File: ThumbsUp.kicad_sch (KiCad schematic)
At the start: 45 parts, among them J10 Raiser_Male, J13 Raiser_Female, J14 Raiser_Male, J19 Raiser_Female, J1L1 PJ-3200B, J1R1 PJ-3200B, J33 Raiser_Male, J34 Raiser_Female, J35 Raiser_Male, J38 Raiser_Female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

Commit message: K12: Placed the touchpad, todo: tracks
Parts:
- added J1, J2: 52559-1233, KiCad:525591233, symbol ThumbsUp-rescue:52559-1233-52559-1233
- added R1, R2, R4, R5: 4.7k, Resistor_SMD:R_0805_2012Metric, symbol Device:R_Small
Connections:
- net GND: now also J1.11, J2.11
- net SDA: now reaches U1.5 (SDA)
- net SDA: now also J1.10, J2.10, R1.1, R5.1
- net SCL: now reaches U1.6 (SCL)
- net SCL: now also J1.9, J2.9, R2.2, R4.2
- new net +3.3V: R1.2, R2.1, R4.1, R5.2
- new net VCC: J1.12, J2.12
- no-connect marks 0 -> 24
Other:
- note added: "Cirque Trackpad Connectors"
- note added: "Dummy network for the shielding/fill-in areas, separating them from the ground line."
- note added: "Pull-up for Cirque Trackpad Resistors are repeated twice - to place their location on both sides."
- moved on the sheet: JP1, R17

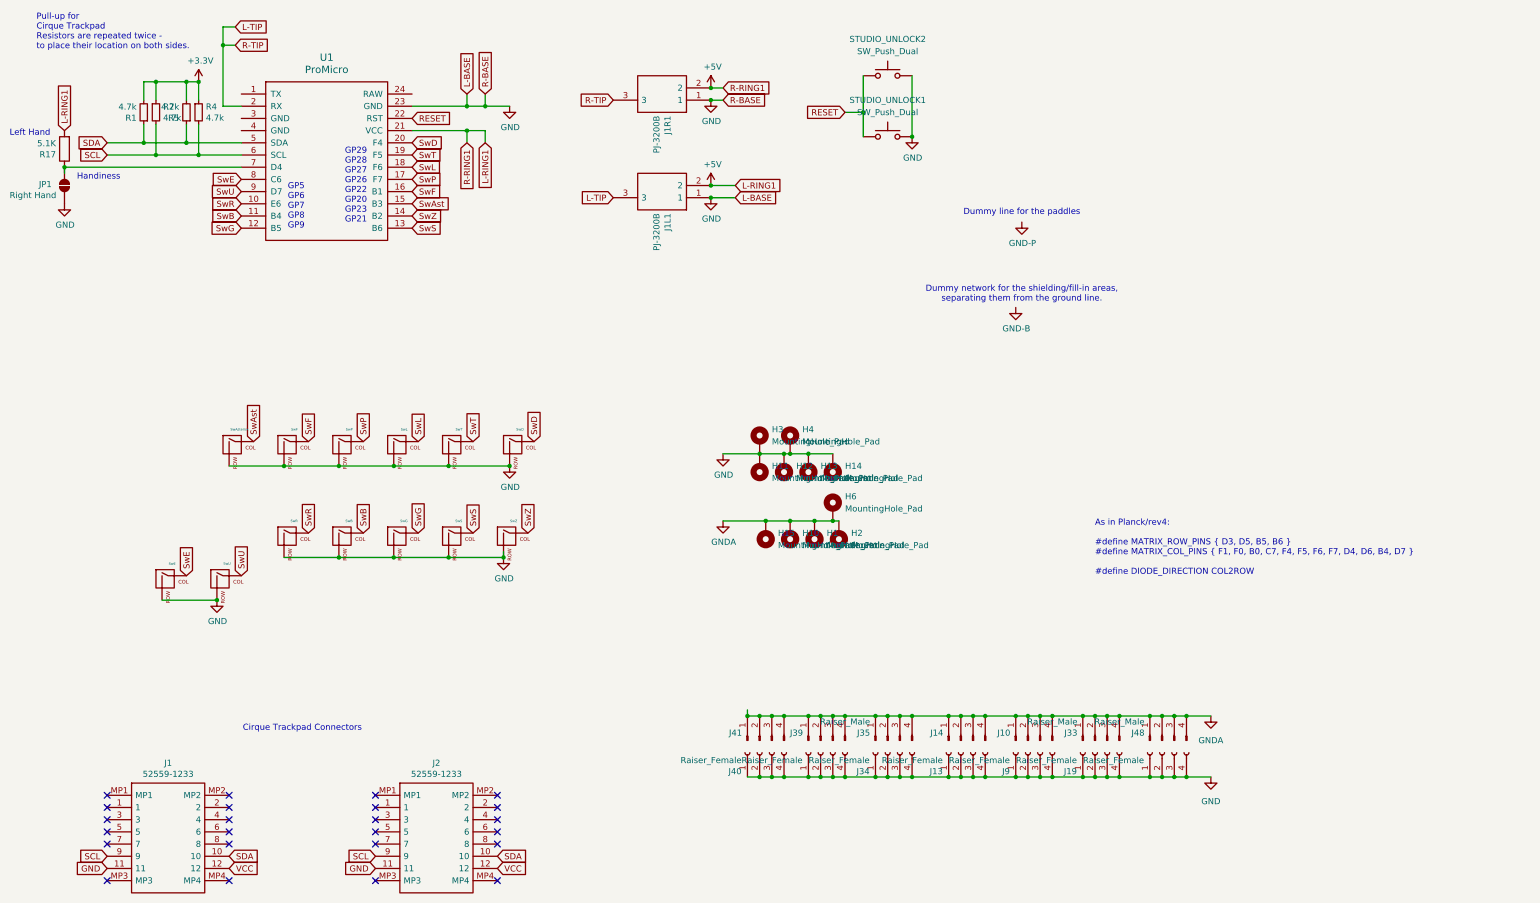
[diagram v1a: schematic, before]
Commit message: K12: Placed the tracks, text, etc. TODO: generate Gerbers.
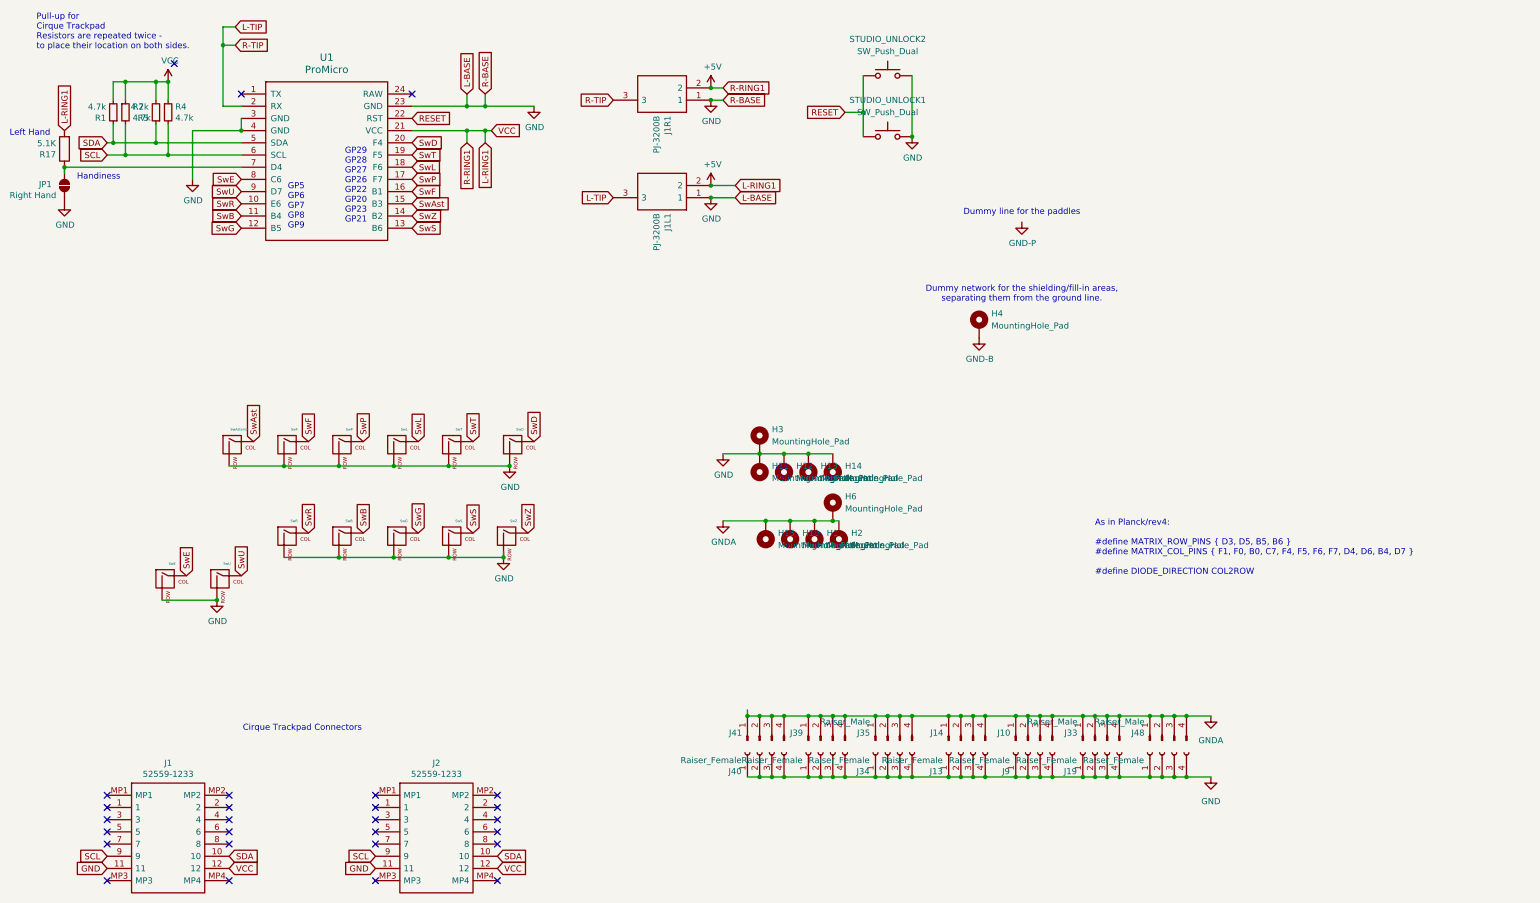
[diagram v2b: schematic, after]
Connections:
- net +3.3V is gone; now on net +5V: R1.2, R2.1, R4.1, R5.2
- net VCC is gone; now on net +5V: J1.12, J2.12
- net GND: now also U1.3 (GND), U1.4 (GND); no longer H4.1
- net GND-B: now also H4.1
- no-connect marks 24 -> 27
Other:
- moved on the sheet: H4, R1, R2, R4, R5

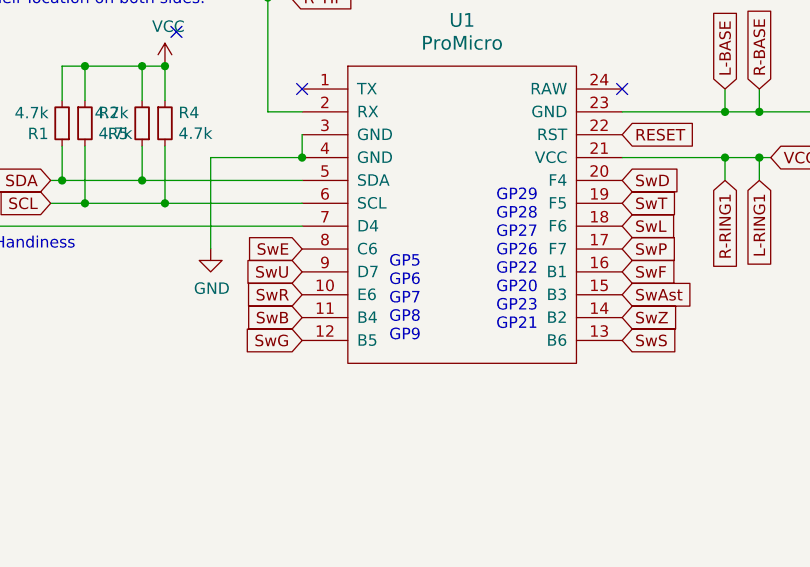
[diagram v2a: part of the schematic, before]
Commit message: K12: Added pictures of rev.3.
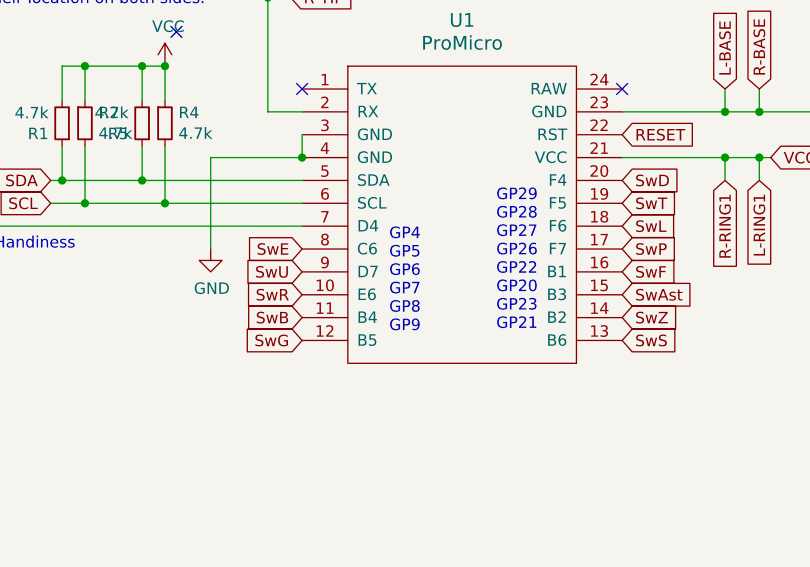
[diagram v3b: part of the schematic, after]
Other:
- note added: "GP4 GP5 GP6 GP7 GP8 GP9"
- note removed: "GP5 GP6 GP7 GP8 GP9"
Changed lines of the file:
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@@
 		)
 	)
-	(text "GP5\nGP6\nGP7\nGP8\nGP9"
+	(text "GP4\nGP5\nGP6\nGP7\nGP8\nGP9"
 		(exclude_from_sim no)
-		(at 320.04 226.568 0)
+		(at 320.04 224.536 0)
 		(effects
 			(font

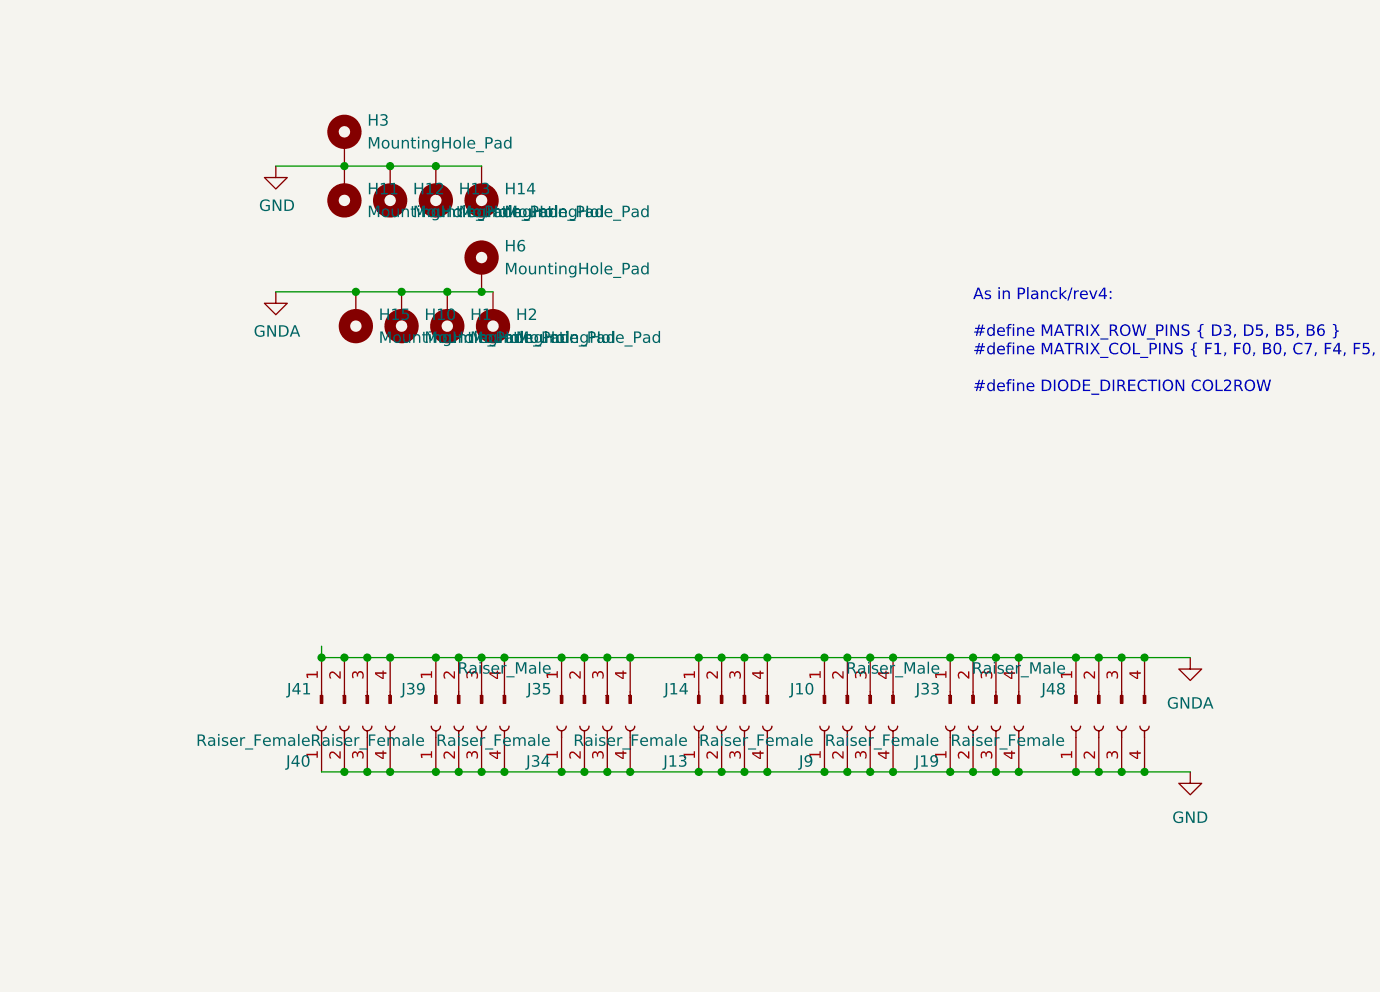
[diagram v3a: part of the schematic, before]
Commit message: v12: Replaced pin headers/sockets with stand-offs..
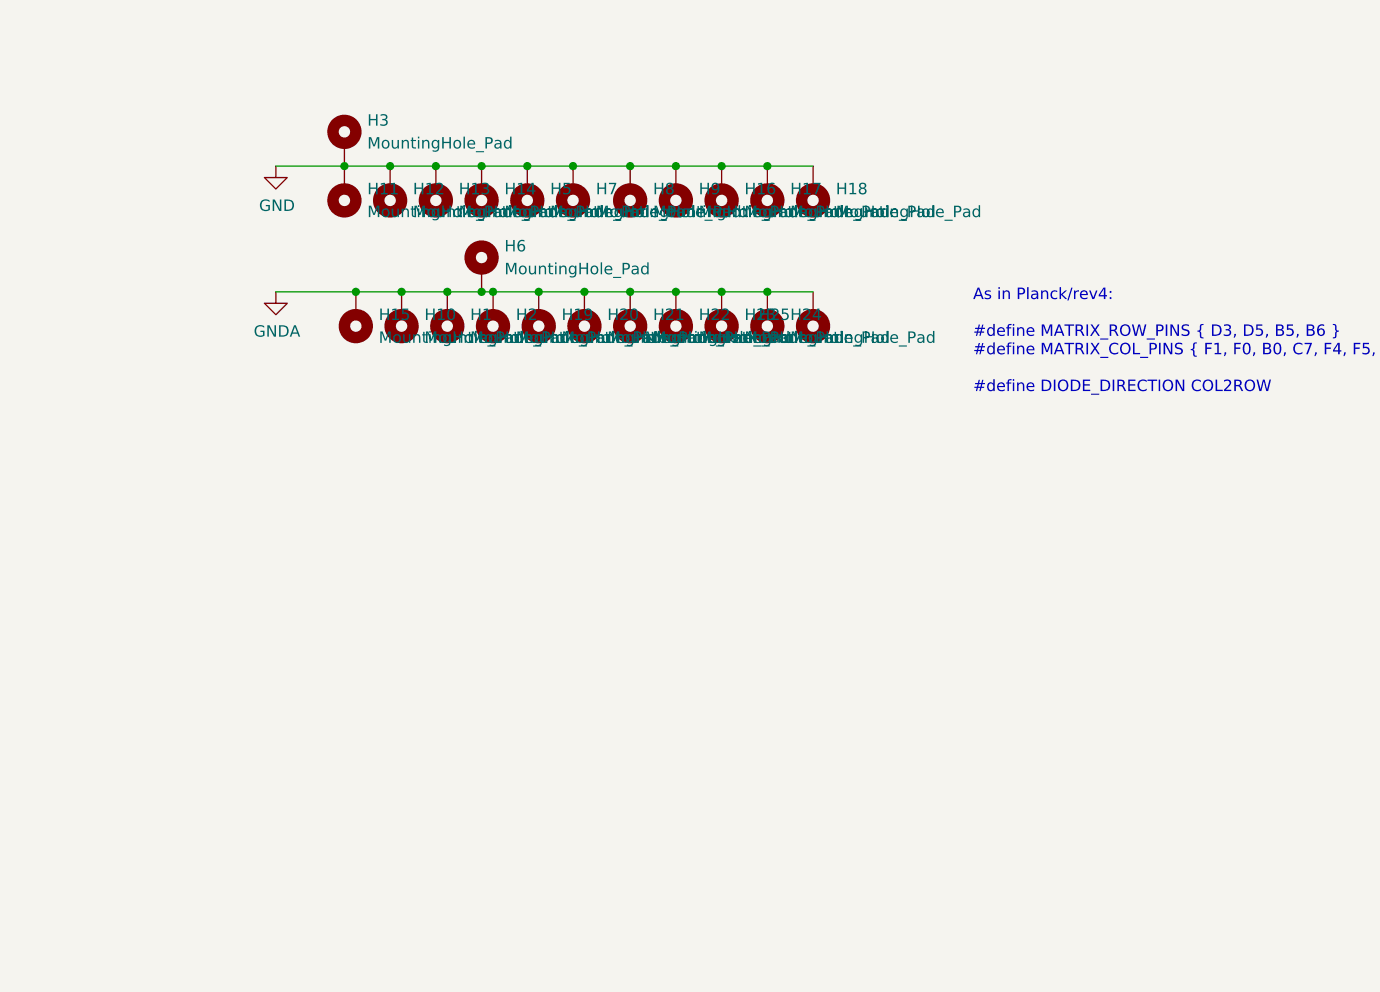
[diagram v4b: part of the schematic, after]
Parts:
- removed J10, J14, J33, J35, J39, J41, J48: Raiser_Male, Connector_PinHeader_2.54mm:PinHeader_1x04_P2.54mm_Vertical, symbol Connector:Conn_01x04_Male
- removed J13, J19, J34, J38, J40, J47, J9: Raiser_Female, Connector_PinSocket_2.54mm:PinSocket_1x04_P2.54mm_Vertical, symbol Connector:Conn_01x04_Female
- added H16, H17, H18, H19, H20, H21, H22, H23, H24, H25, H5, H7, H8, H9: MountingHole_Pad, MountingHole:MountingHole_3.5mm_Pad, symbol Mechanical:MountingHole_Pad
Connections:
- net GND: now also H16.1, H17.1, H18.1, H5.1, H7.1, H8.1, H9.1
- net GNDA: now also H19.1, H20.1, H21.1, H22.1, H23.1, H24.1, H25.1

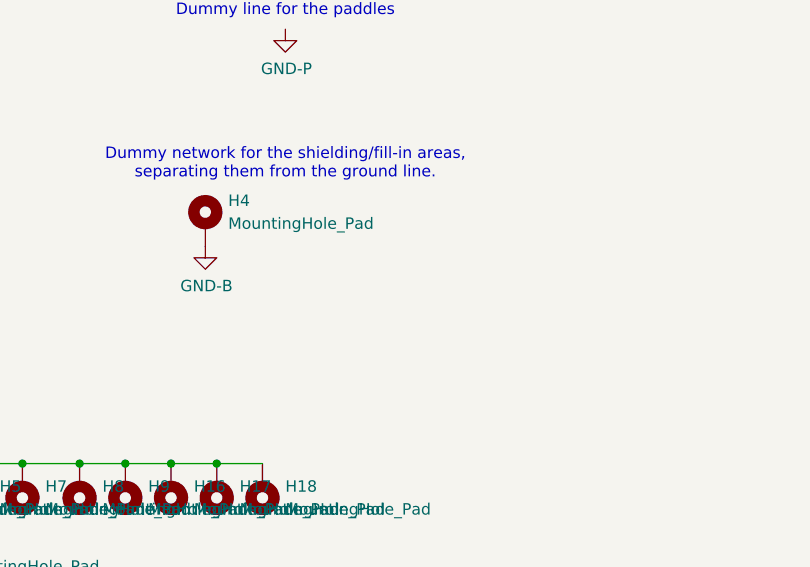
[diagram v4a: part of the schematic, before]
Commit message: v12: Moving the thumb keys around.
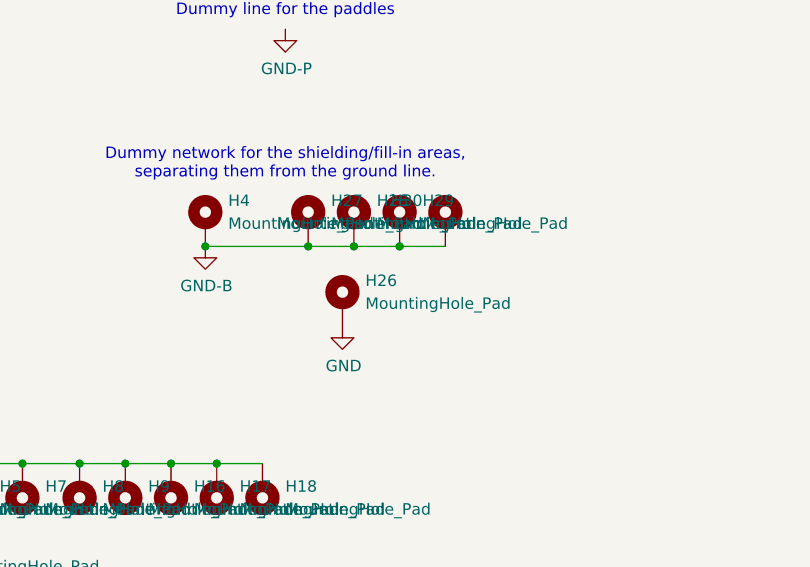
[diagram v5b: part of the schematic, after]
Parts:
- added H26, H27, H28, H29, H30: MountingHole_Pad, MountingHole:MountingHole_4.5mm_Pad, symbol Mechanical:MountingHole_Pad
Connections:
- net GND: now also H26.1
- net GND-B: now also H27.1, H28.1, H29.1, H30.1
